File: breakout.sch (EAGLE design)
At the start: 36 parts, among them U1 ATMEGA128RFA1, U2 FT232RL

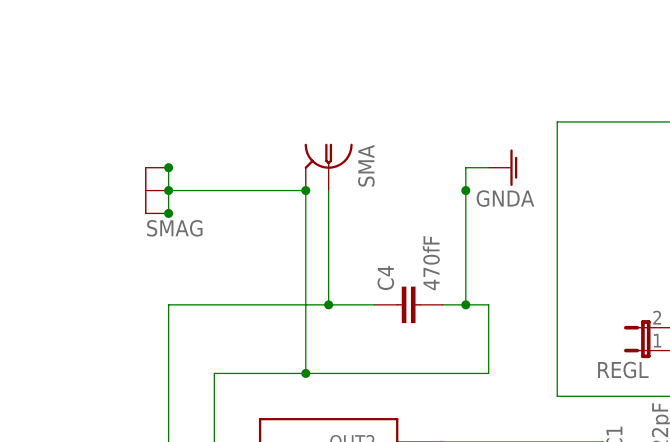
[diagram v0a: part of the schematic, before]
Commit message: Switch to using a u.fl connector from SMA
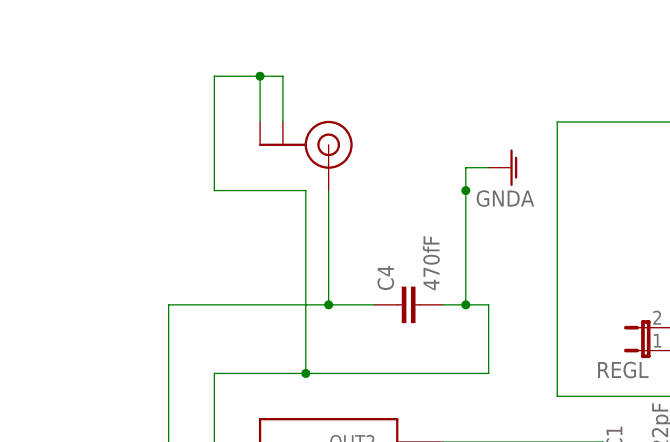
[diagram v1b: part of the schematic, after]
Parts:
- removed SMA: LTI-SASF54GT, con-coax:LTI-SASF54GT
- added U$6: U.FL, SparkFun-Connectors:U.FL
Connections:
- net GNDA: now also U$6.GND@0, U$6.GND@1; no longer SMAG$1.GND, SMAG.GND@1, SMAG.GND@2, SMAG.GND@3
- net SMA: now also U$6.SIGNAL; no longer SMAG$1.1
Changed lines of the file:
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@@
 <layer number="144" name="Drill_legend" color="7" fill="1" visible="no" active="yes"/>
 <layer number="151" name="HeatSink" color="7" fill="1" visible="no" active="yes"/>
+<layer number="199" name="Contour" color="7" fill="1" visible="yes" active="yes"/>
 <layer number="200" name="200bmp" color="1" fill="10" visible="no" active="yes"/>
 <layer number="201" name="201bmp" color="2" fill="10" visible="no" active="yes"/>
@@
 <part name="PORTB" library="SparkFun" deviceset="M08" device="1X08"/>
 <part name="GND20" library="supply1" deviceset="GNDA" device=""/>
-<part name="SMA" library="con-coax" deviceset="LTI-SASF54GT" device="" value=""/>
 <part name="GND7" library="supply1" deviceset="GND" device=""/>
 <part name="RSTON" library="led" deviceset="LED" device="CHIPLED_0603"/>
@@
 <part name="GND27" library="supply1" deviceset="GND" device=""/>
 <part name="GND22" library="supply1" deviceset="GND" device=""/>
+<part name="U$6" library="SparkFun-Connectors" deviceset="U.FL" device=""/>
 </parts>
 <sheets>
@@
 <instance part="PORTB" gate="G$1" x="220.98" y="119.38" rot="R180"/>
 <instance part="GND20" gate="1" x="78.74" y="55.88" rot="R270"/>
-<instance part="SMA" gate="G$1" x="12.7" y="144.78" rot="R270"/>
-<instance part="SMA" gate="G" x="-7.62" y="144.78"/>
 <instance part="GND7" gate="1" x="30.48" y="71.12" rot="R90"/>
 <instance part="RSTON" gate="G$1" x="111.76" y="99.06" rot="R270"/>
@@
 <instance part="GND27" gate="1" x="106.68" y="129.54" rot="R180"/>
 <instance part="GND22" gate="1" x="124.46" y="147.32" rot="R90"/>
+<instance part="U$6" gate="G$1" x="12.7" y="147.32" rot="R270"/>
 </instances>
 <busses>
@@
 <wire x1="27.94" y1="144.78" x2="27.94" y2="142.24" width="0.1524" layer="91"/>
 <wire x1="0" y1="121.92" x2="0" y2="111.76" width="0.1524" layer="91"/>
-<wire x1="10.16" y1="142.24" x2="-5.08" y2="142.24" width="0.1524" layer="91"/>
-<wire x1="-5.08" y1="144.78" x2="-5.08" y2="142.24" width="0.1524" layer="91"/>
-<wire x1="-5.08" y1="142.24" x2="-5.08" y2="139.7" width="0.1524" layer="91"/>
 <wire x1="0" y1="121.92" x2="10.16" y2="121.92" width="0.1524" layer="91"/>
 <wire x1="10.16" y1="121.92" x2="10.16" y2="142.24" width="0.1524" layer="91"/>
@@
 <wire x1="30.48" y1="121.92" x2="30.48" y2="129.54" width="0.1524" layer="91"/>
 <wire x1="27.94" y1="142.24" x2="27.94" y2="129.54" width="0.1524" layer="91"/>
-<junction x="-5.08" y="142.24"/>
-<junction x="-5.08" y="144.78"/>
-<junction x="-5.08" y="139.7"/>
-<junction x="10.16" y="142.24"/>
 <junction x="10.16" y="121.92"/>
 <junction x="27.94" y="129.54"/>
@@
 <pinref part="GND9" gate="1" pin="GNDA"/>
 <pinref part="B1" gate="G$1" pin="GNDDC"/>
-<pinref part="SMA" gate="G$1" pin="GND"/>
-<pinref part="SMA" gate="G" pin="GND@2"/>
-<pinref part="SMA" gate="G" pin="GND@1"/>
-<pinref part="SMA" gate="G" pin="GND@3"/>
 <pinref part="C4" gate="G$1" pin="2"/>
+<wire x1="10.16" y1="142.24" x2="0" y2="142.24" width="0.1524" layer="91"/>
+<wire x1="0" y1="142.24" x2="0" y2="154.94" width="0.1524" layer="91"/>
+<pinref part="U$6" gate="G$1" pin="GND@1"/>
+<wire x1="0" y1="154.94" x2="5.08" y2="154.94" width="0.1524" layer="91"/>
+<wire x1="5.08" y1="154.94" x2="5.08" y2="149.86" width="0.1524" layer="91"/>
+<pinref part="U$6" gate="G$1" pin="GND@0"/>
+<wire x1="5.08" y1="154.94" x2="7.62" y2="154.94" width="0.1524" layer="91"/>
+<wire x1="7.62" y1="154.94" x2="7.62" y2="149.86" width="0.1524" layer="91"/>
+<junction x="5.08" y="154.94"/>
 </segment>
 <segment>
@@
 <junction x="12.7" y="129.54"/>
 <pinref part="C4" gate="G$1" pin="1"/>
-<pinref part="SMA" gate="G$1" pin="1"/>
 <pinref part="B1" gate="G$1" pin="IN"/>
-</segment>
-</net>
+<pinref part="U$6" gate="G$1" pin="SIGNAL"/>
+</segment>
+</net>
